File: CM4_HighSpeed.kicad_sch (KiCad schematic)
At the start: 4 parts, among them J10 Conn_01x22

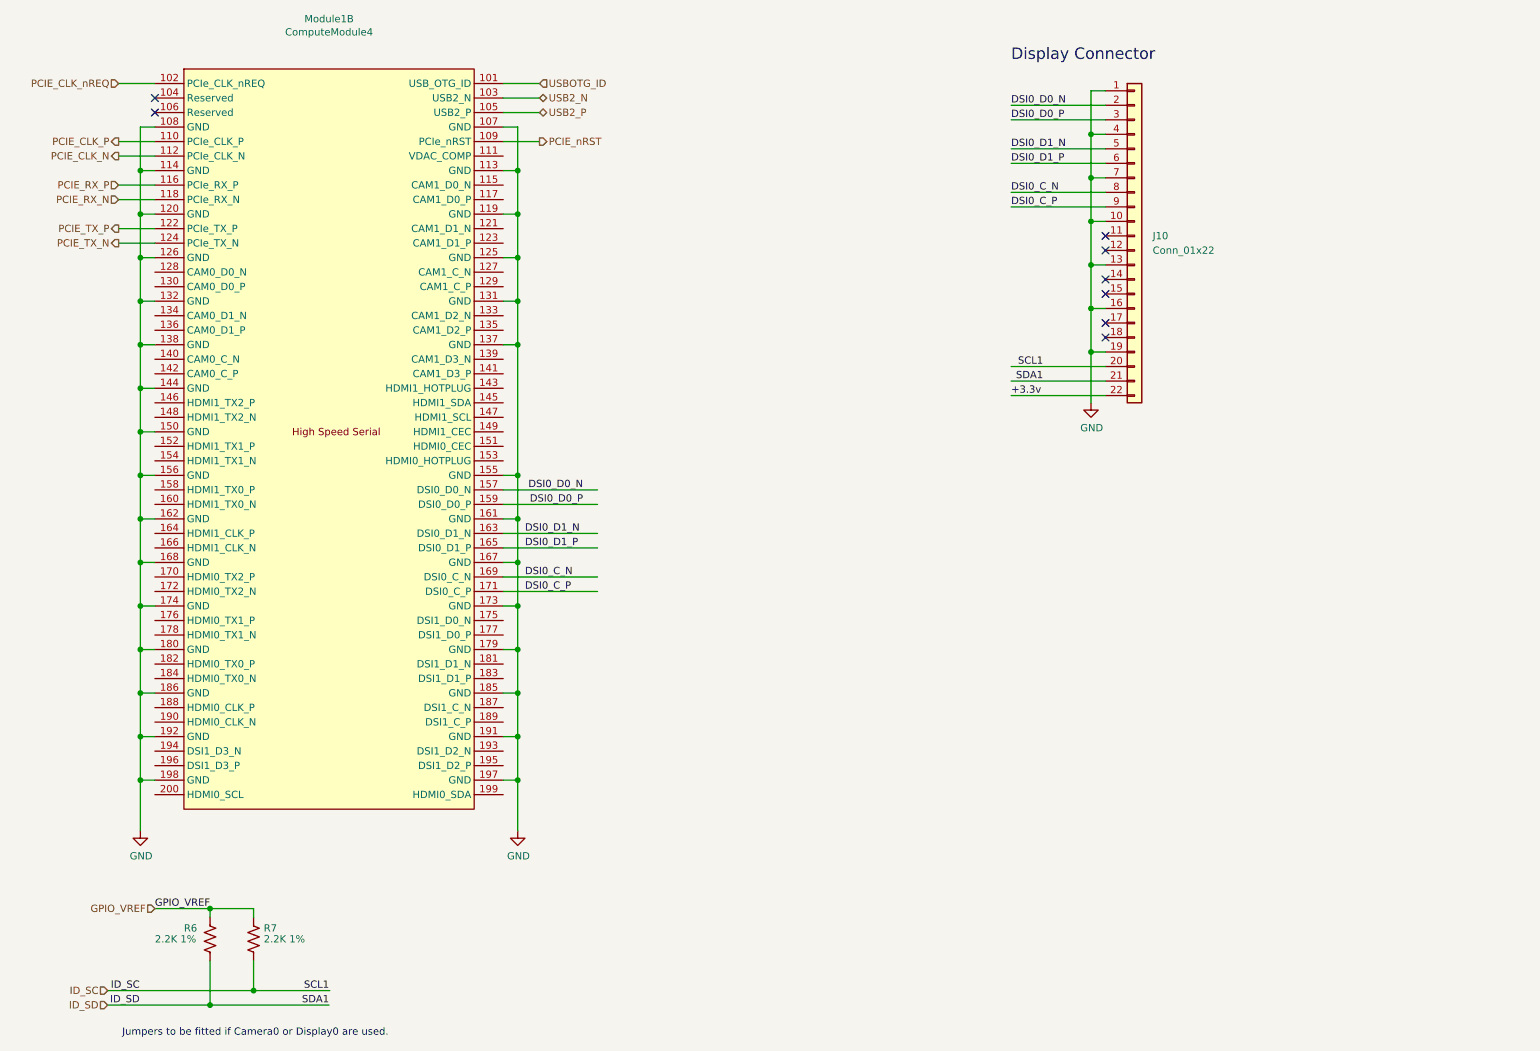
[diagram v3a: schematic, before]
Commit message: resolved some schematic-board errors. switched to tap-on-top ethernet.
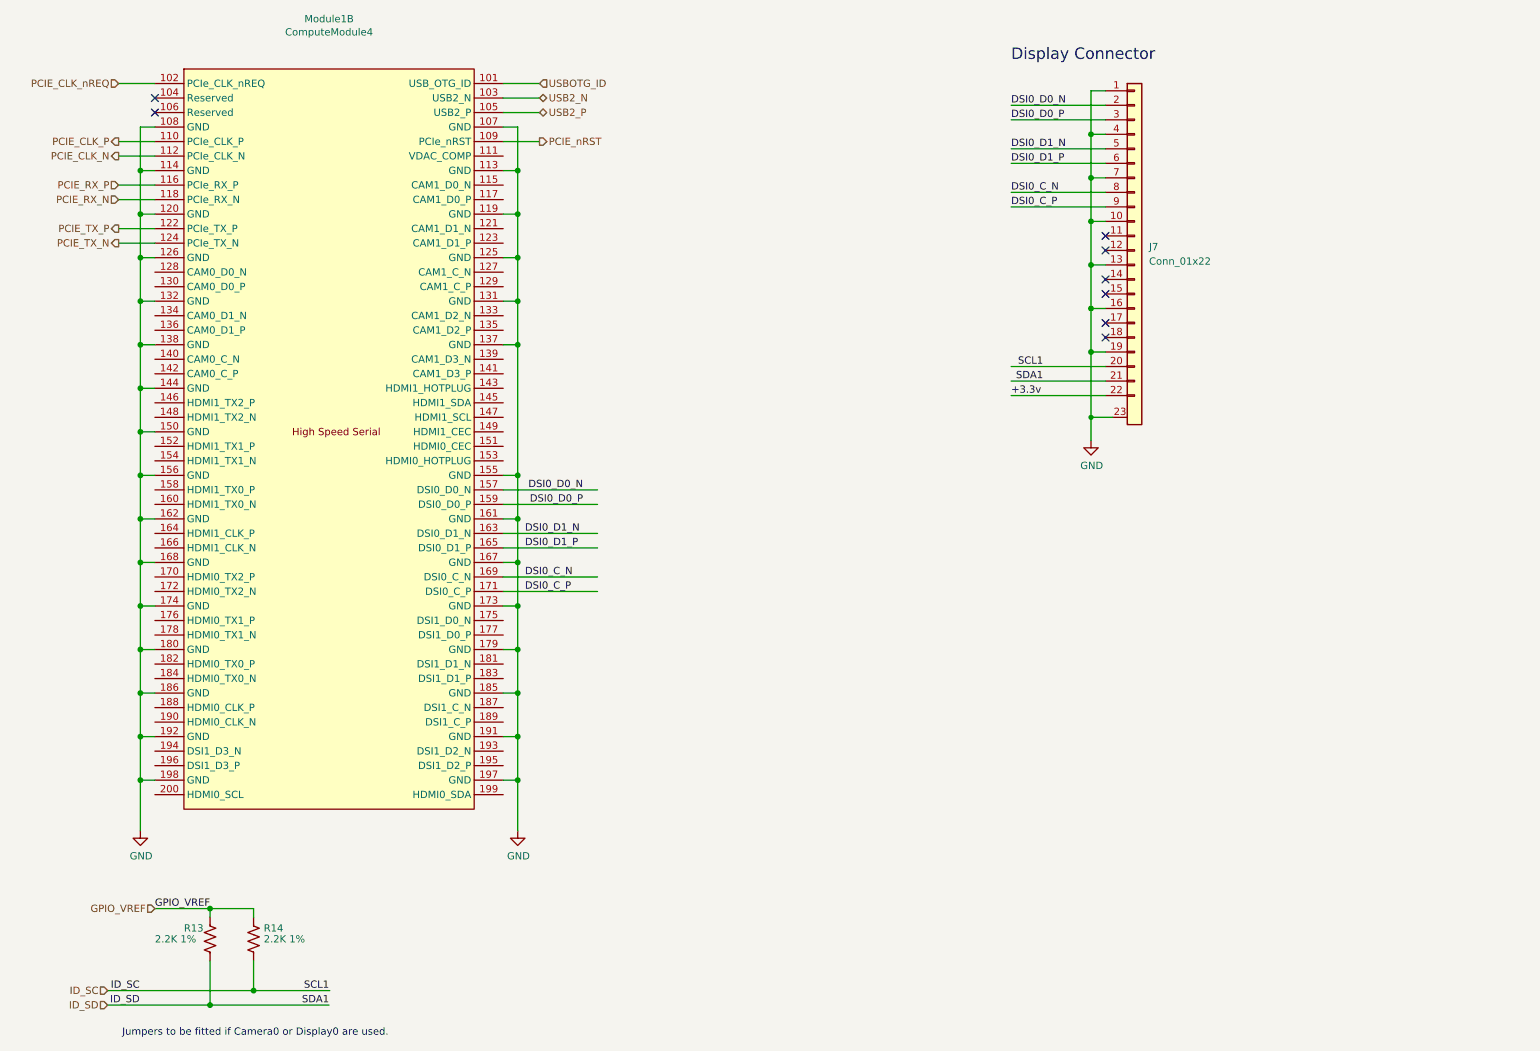
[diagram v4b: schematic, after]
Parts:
- J7: renamed from J10; symbol Connector_Generic:Conn_01x22 -> bitcart:Conn_01x22
- renumbered R6 to R13, R7 to R14
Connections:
- net GND: now also J7.23, J7.24, J7.25, J7.26
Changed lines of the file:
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@@
   (junction (at 105.41 110.49) (diameter 1.016) (color 0 0 0 0)
+  )
+  (junction (at 205.74 85.09) (diameter 0) (color 0 0 0 0)
   )
   (junction (at 105.41 49.53) (diameter 1.016) (color 0 0 0 0)
@@
     (stroke (width 0) (type solid))
   )
+  (wire (pts (xy 205.74 85.09) (xy 209.55 85.09))
+    (stroke (width 0) (type default))
+  )
   (wire (pts (xy 39.37 133.35) (xy 39.37 140.97))
     (stroke (width 0) (type solid))
@@
     (stroke (width 0) (type solid))
   )
+  (wire (pts (xy 205.74 85.09) (xy 205.74 89.154))
+    (stroke (width 0) (type solid))
+  )
   (wire (pts (xy 39.37 118.11) (xy 39.37 125.73))
     (stroke (width 0) (type solid))
@@
     (stroke (width 0) (type solid))
   )
-  (wire (pts (xy 205.74 73.66) (xy 205.74 82.55))
+  (wire (pts (xy 205.74 73.66) (xy 205.74 85.09))
     (stroke (width 0) (type solid))
   )
@@
   (symbol (lib_id "power:GND") (at 105.41 157.48 0) (unit 1)
     (in_bom yes) (on_board yes) (dnp no)
-    (property "Reference" "#PWR0130" (at 105.41 163.83 0)
+    (property "Reference" "#PWR028" (at 105.41 163.83 0)
       (effects (font (size 1.27 1.27)) hide)
     )
@@
       (project "bitcart"
         (path "/e63e39d7-6ac0-4ffd-8aa3-1841a4541b55/00000000-0000-0000-0000-00005cff70b1"
-          (reference "#PWR0130") (unit 1)
+          (reference "#PWR028") (unit 1)
         )
       )
@@
   (symbol (lib_id "power:GND") (at 39.37 157.48 0) (unit 1)
     (in_bom yes) (on_board yes) (dnp no)
-    (property "Reference" "#PWR0131" (at 39.37 163.83 0)
+    (property "Reference" "#PWR027" (at 39.37 163.83 0)
       (effects (font (size 1.27 1.27)) hide)
     )
@@
       (project "bitcart"
         (path "/e63e39d7-6ac0-4ffd-8aa3-1841a4541b55/00000000-0000-0000-0000-00005cff70b1"
-          (reference "#PWR0131") (unit 1)
+          (reference "#PWR027") (unit 1)
         )
       )
     )
   )
-  (symbol (lib_id "power:GND") (at 205.74 82.55 0) (unit 1)
+  (symbol (lib_id "power:GND") (at 205.74 89.154 0) (unit 1)
     (in_bom yes) (on_board yes) (dnp no)
-    (property "Reference" "#PWR0133" (at 205.74 88.9 0)
-      (effects (font (size 1.27 1.27)) hide)
-    )
-    (property "Value" "GND" (at 205.867 86.9442 0)
+    (property "Reference" "#PWR029" (at 205.74 95.504 0)
+      (effects (font (size 1.27 1.27)) hide)
+    )
+    (property "Value" "GND" (at 205.867 93.5482 0)
       (effects (font (size 1.27 1.27)))
     )
-    (property "Footprint" "" (at 205.74 82.55 0)
-      (effects (font (size 1.27 1.27)) hide)
-    )
-    (property "Datasheet" "" (at 205.74 82.55 0)
+    (property "Footprint" "" (at 205.74 89.154 0)
+      (effects (font (size 1.27 1.27)) hide)
+    )
+    (property "Datasheet" "" (at 205.74 89.154 0)
       (effects (font (size 1.27 1.27)) hide)
     )
@@
       (project "bitcart"
         (path "/e63e39d7-6ac0-4ffd-8aa3-1841a4541b55/00000000-0000-0000-0000-00005cff70b1"
-          (reference "#PWR0133") (unit 1)
+          (reference "#PWR029") (unit 1)
         )
       )
@@
   (symbol (lib_id "Device:R_US") (at 51.562 176.403 0) (unit 1)
     (in_bom yes) (on_board yes) (dnp no)
-    (property "Reference" "R6" (at 46.99 174.498 0)
+    (property "Reference" "R13" (at 46.99 174.498 0)
       (effects (font (size 1.27 1.27)) (justify left))
     )
@@
       (project "bitcart"
         (path "/e63e39d7-6ac0-4ffd-8aa3-1841a4541b55/00000000-0000-0000-0000-00005cff70b1"
-          (reference "R6") (unit 1)
+          (reference "R13") (unit 1)
         )
       )
@@
   (symbol (lib_id "Device:R_US") (at 59.182 176.403 0) (unit 1)
     (in_bom yes) (on_board yes) (dnp no)
-    (property "Reference" "R7" (at 60.96 174.498 0)
+    (property "Reference" "R14" (at 60.96 174.498 0)
       (effects (font (size 1.27 1.27)) (justify left))
     )
@@
       (project "bitcart"
         (path "/e63e39d7-6ac0-4ffd-8aa3-1841a4541b55/00000000-0000-0000-0000-00005cff70b1"
-          (reference "R7") (unit 1)
+          (reference "R14") (unit 1)
         )
       )
@@
     )
   )
-  (symbol (lib_id "Connector_Generic:Conn_01x22") (at 213.36 53.34 0) (unit 1)
+  (symbol (lib_id "bitcart:Conn_01x22") (at 213.36 53.34 0) (unit 1)
     (in_bom yes) (on_board yes) (dnp no) (fields_autoplaced)
-    (property "Reference" "J10" (at 216.535 53.34 0)
+    (property "Reference" "J7" (at 215.9 55.245 0)
       (effects (font (size 1.27 1.27)) (justify left))
     )
-    (property "Value" "Conn_01x22" (at 216.535 55.88 0)
+    (property "Value" "Conn_01x22" (at 215.9 57.785 0)
       (effects (font (size 1.27 1.27)) (justify left))
     )
@@
       (effects (font (size 1.27 1.27)) hide)
     )
+    (pin "26")
     (pin "1")
     (pin "10")
@@
     (pin "21")
     (pin "22")
+    (pin "23")
+    (pin "24")
+    (pin "25")
     (pin "3")
     (pin "4")
@@
       (project "bitcart"
         (path "/e63e39d7-6ac0-4ffd-8aa3-1841a4541b55/00000000-0000-0000-0000-00005cff70b1"
-          (reference "J10") (unit 1)
+          (reference "J7") (unit 1)
         )
       )

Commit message: pulled in bitcrane fan and data connectors and edge cuts. most placement done. started routing
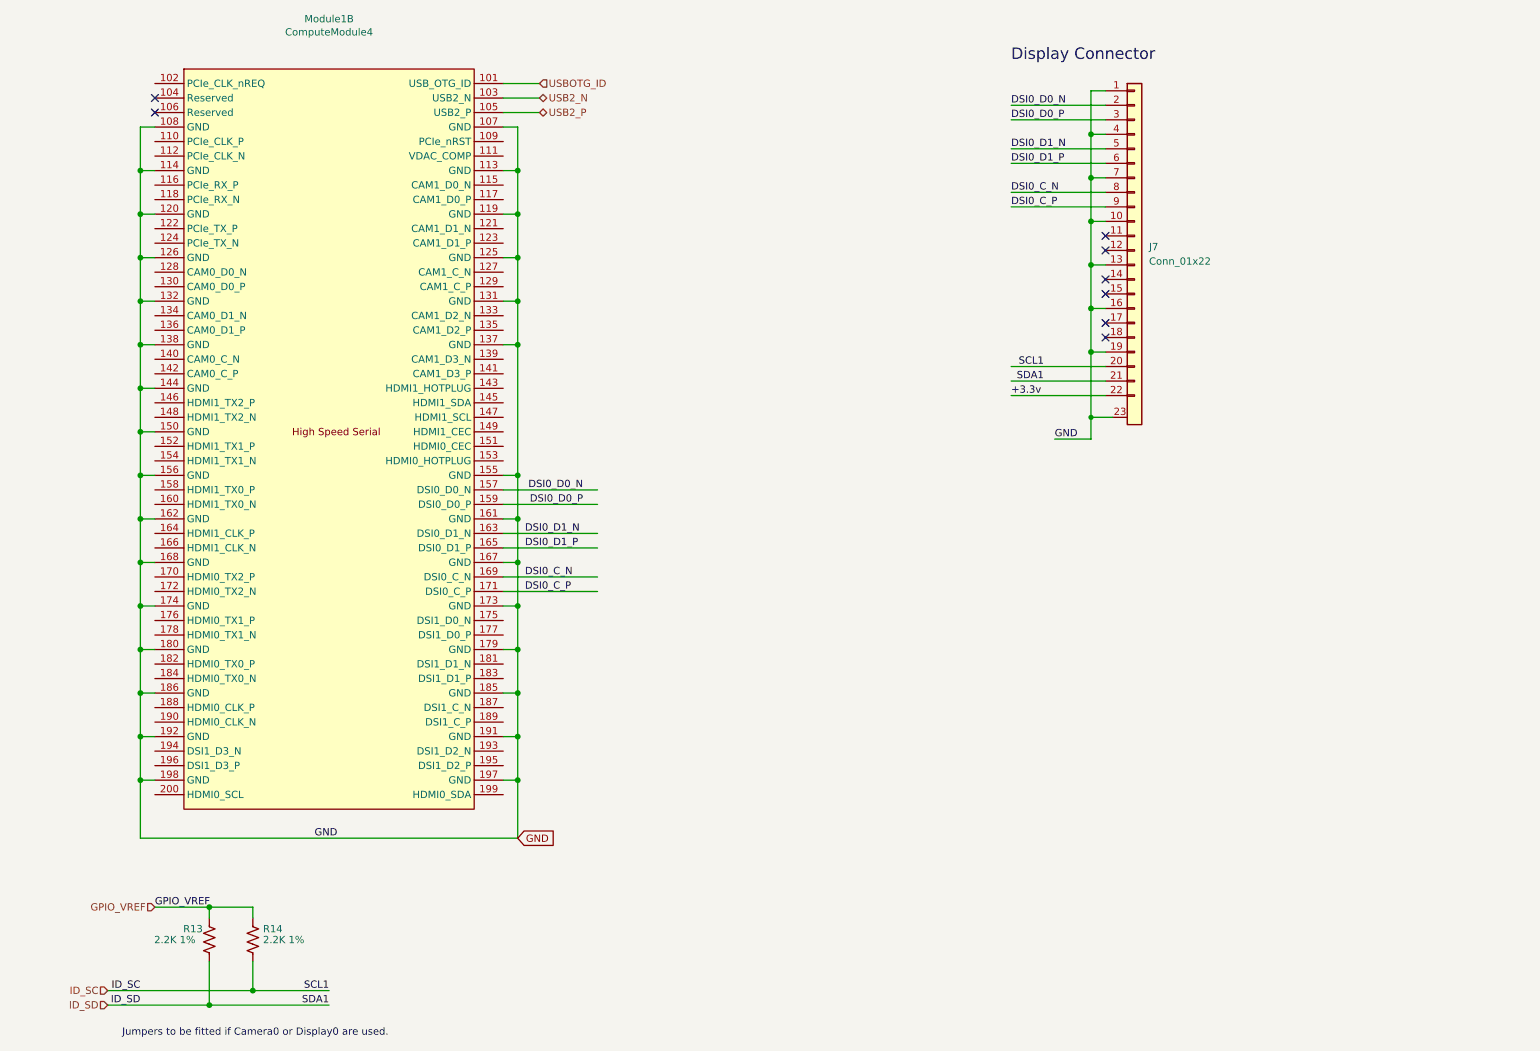
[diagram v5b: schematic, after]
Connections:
- net PCIE_CLK_N: no longer names the net of Module1.112 (PCIe_CLK_N)
- net PCIE_CLK_P: no longer names the net of Module1.110 (PCIe_CLK_P)
- net PCIE_CLK_nREQ: no longer names the net of Module1.102 (PCIe_CLK_nREQ)
- net PCIE_RX_N: no longer names the net of Module1.118 (PCIe_RX_N)
- net PCIE_RX_P: no longer names the net of Module1.116 (PCIe_RX_P)
- net PCIE_TX_N: no longer names the net of Module1.124 (PCIe_TX_N)
- net PCIE_TX_P: no longer names the net of Module1.122 (PCIe_TX_P)
- net PCIE_nRST: no longer names the net of Module1.109 (PCIe_nRST)

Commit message: lots of routing. lots more to do
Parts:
- R13, R14: value 2.2K 1% -> 2.2k 1%
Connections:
- net +3.3v renamed 3V3
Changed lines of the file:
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@@
     (effects (font (size 1.27 1.27)) (justify left bottom))
   )
-  (label "+3.3v" (at 191.77 81.28 0) (fields_autoplaced)
+  (label "3V3" (at 191.77 81.28 0) (fields_autoplaced)
     (effects (font (size 1.27 1.27)) (justify left bottom))
   )
@@
       (effects (font (size 1.27 1.27)) (justify left))
     )
-    (property "Value" "2.2K 1%" (at 41.783 176.53 0)
+    (property "Value" "2.2k 1%" (at 41.783 176.53 0)
       (effects (font (size 1.27 1.27)) (justify left))
     )
@@
       (effects (font (size 1.27 1.27)) (justify left))
     )
-    (property "Value" "2.2K 1%" (at 60.833 176.53 0)
+    (property "Value" "2.2k 1%" (at 60.833 176.53 0)
       (effects (font (size 1.27 1.27)) (justify left))
     )
